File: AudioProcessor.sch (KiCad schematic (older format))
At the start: 17 parts

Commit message: 3v3 über LDO von BMS enablen. Bluetooth hinzugefügt
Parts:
- added J601: AudioJack3_Ground, symbol Connector:AudioJack3_Ground
- added R604, R605, R606, R607: 100R, symbol Device:R_Small
- added R608, R609: 47R, symbol Device:R_Small
- C607, C608, C609, C610: renamed from C?; value 1nF -> 100nF
- gave numbers to parts that had none: 13
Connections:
- net labels added: AUX_DETECT, AUX_GND, BT_GND, BT_LEFT, BT_RIGHT
- net labels removed: BT_L, BT_R
- wire segments 44 -> 63
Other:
- note added: "Folenkondensatoren wegen Akustik"
- note added: "I2C Isolator?"
- note added: "f_cutoff = 1/(100nF*100R) = 15.9kHz"
- moved on the sheet: C603, C604, C605, C606

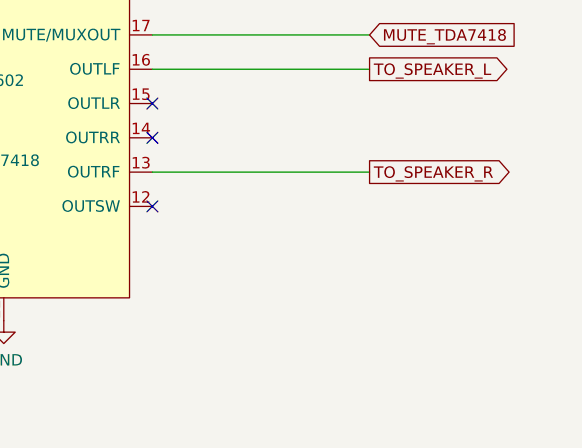
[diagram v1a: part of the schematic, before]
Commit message: power schalter und taser hinzugefügt. Selbsthaltung LDO hinzugefügt. Gain Potis hinzugefügt, Separater Ground für Audio Lines
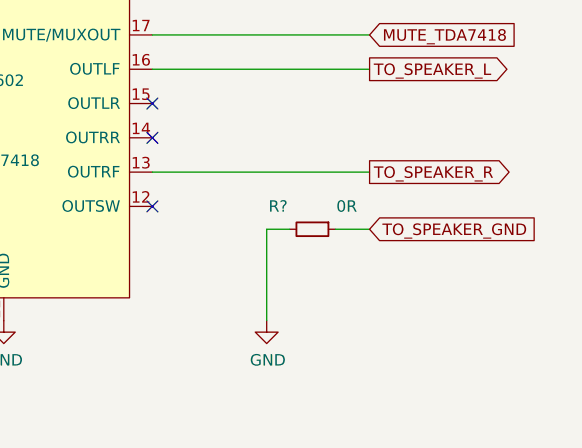
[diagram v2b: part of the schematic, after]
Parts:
- added R?: 0R, symbol Device:R_Small
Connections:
- net labels added: TO_SPEAKER_GND
- wire segments 63 -> 66
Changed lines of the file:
@@
 Wire Wire Line
 	2100 4750 1600 4750
+Text GLabel 9050 5100 2    50   Input ~ 0
+TO_SPEAKER_GND
+$Comp
+L Device:R_Small R?
+U 1 1 5E923218
+P 8800 5100
+F 0 "R?" V 8700 4950 50  0000 C CNN
+F 1 "0R" V 8700 5250 50  0000 C CNN
+F 2 "" H 8800 5100 50  0001 C CNN
+F 3 "~" H 8800 5100 50  0001 C CNN
+	1    8800 5100
+	0    1    1    0
+$EndComp
+Wire Wire Line
+	9050 5100 8900 5100
+$Comp
+L power:GND #PWR?
+U 1 1 5E924643
+P 8600 5500
+F 0 "#PWR?" H 8600 5250 50  0001 C CNN
+F 1 "GND" H 8605 5327 50  0000 C CNN
+F 2 "" H 8600 5500 50  0001 C CNN
+F 3 "" H 8600 5500 50  0001 C CNN
+	1    8600 5500
+	1    0    0    -1
+$EndComp
+Wire Wire Line
+	8700 5100 8600 5100
+Wire Wire Line
+	8600 5100 8600 5500
 $EndSCHEMATC

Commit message: Schaltplan fertig. Fertig für review
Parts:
- removed R?: 0R, symbol Device:R_Small
- added R? (x2): 47K, symbol Device:R_Small
- added R?: DNP, symbol Device:R_Small
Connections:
- net labels added: +3V3, GNDA
- net labels removed: AUX_GND, BT_GND, TO_SPEAKER_GND
- wire segments 66 -> 67
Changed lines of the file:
@@
 Wire Wire Line
 	5900 4050 6350 4050
-$Comp
-L power:GND #PWR0159
-U 1 1 5EA68AB5
-P 7450 5500
-F 0 "#PWR0159" H 7450 5250 50  0001 C CNN
-F 1 "GND" H 7455 5327 50  0000 C CNN
-F 2 "" H 7450 5500 50  0001 C CNN
-F 3 "" H 7450 5500 50  0001 C CNN
-	1    7450 5500
-	1    0    0    -1
-$EndComp
 Wire Wire Line
 	7450 3700 7450 3450
@@
 Text GLabel 9050 4250 2    50   Input ~ 0
 MUTE_TDA7418
-Wire Wire Line
-	9050 4250 8100 4250
 NoConn ~ 8100 4550
 NoConn ~ 8100 4700
@@
 	6650 5350 6650 5550
 $Comp
-L power:GND #PWR0165
-U 1 1 5EACAB6F
-P 6650 5750
-F 0 "#PWR0165" H 6650 5500 50  0001 C CNN
-F 1 "GND" H 6655 5577 50  0000 C CNN
-F 2 "" H 6650 5750 50  0001 C CNN
-F 3 "" H 6650 5750 50  0001 C CNN
-	1    6650 5750
-	1    0    0    -1
-$EndComp
-$Comp
 L power:+9V #PWR0166
 U 1 1 5EACB6B4
@@
 Text Notes 3450 3950 0    89   ~ 0
 I2C Isolator?
-Text GLabel 6250 5750 0    50   Input ~ 0
-BT_GND
 Wire Wire Line
 	6450 5250 6450 5300
@@
 Wire Wire Line
 	6250 5300 6250 5750
-Text GLabel 5850 5650 0    50   Input ~ 0
-AUX_GND
 Wire Wire Line
 	6050 5250 6050 5300
@@
 Wire Wire Line
 	5850 5300 5850 5250
-Wire Wire Line
-	5850 5300 5850 5650
 Connection ~ 5850 5300
 $Comp
@@
 	1    0    0    -1
 $EndComp
-Text GLabel 2100 4850 2    50   Output ~ 0
+Text GLabel 2950 4850 2    50   Output ~ 0
 AUX_DETECT
-Wire Wire Line
-	2100 4850 1600 4850
-Text GLabel 1850 5200 2    50   Output ~ 0
-AUX_GND
-Wire Wire Line
-	1850 5200 1400 5200
 Wire Wire Line
 	1400 5200 1400 5050
@@
 Wire Wire Line
 	2100 4750 1600 4750
-Text GLabel 9050 5100 2    50   Input ~ 0
-TO_SPEAKER_GND
+$Comp
+L power:GNDA #PWR?
+U 1 1 5E90960C
+P 6250 5750
+F 0 "#PWR?" H 6250 5500 50  0001 C CNN
+F 1 "GNDA" H 6255 5577 50  0000 C CNN
+F 2 "" H 6250 5750 50  0001 C CNN
+F 3 "" H 6250 5750 50  0001 C CNN
+	1    6250 5750
+	1    0    0    -1
+$EndComp
+$Comp
+L power:GNDA #PWR?
+U 1 1 5E909649
+P 5850 5750
+F 0 "#PWR?" H 5850 5500 50  0001 C CNN
+F 1 "GNDA" H 5855 5577 50  0000 C CNN
+F 2 "" H 5850 5750 50  0001 C CNN
+F 3 "" H 5850 5750 50  0001 C CNN
+	1    5850 5750
+	1    0    0    -1
+$EndComp
+Wire Wire Line
+	5850 5300 5850 5750
+$Comp
+L power:GND #PWR?
+U 1 1 5E90AB64
+P 6650 5750
+F 0 "#PWR?" H 6650 5500 50  0001 C CNN
+F 1 "GND" H 6655 5577 50  0000 C CNN
+F 2 "" H 6650 5750 50  0001 C CNN
+F 3 "" H 6650 5750 50  0001 C CNN
+	1    6650 5750
+	1    0    0    -1
+$EndComp
+$Comp
+L power:GND #PWR?
+U 1 1 5E90D4CD
+P 7450 5750
+F 0 "#PWR?" H 7450 5500 50  0001 C CNN
+F 1 "GND" H 7455 5577 50  0000 C CNN
+F 2 "" H 7450 5750 50  0001 C CNN
+F 3 "" H 7450 5750 50  0001 C CNN
+	1    7450 5750
+	1    0    0    -1
+$EndComp
+Wire Wire Line
+	7450 5750 7450 5500
 $Comp
 L Device:R_Small R?
-U 1 1 5E923218
-P 8800 5100
-F 0 "R?" V 8700 4950 50  0000 C CNN
-F 1 "0R" V 8700 5250 50  0000 C CNN
-F 2 "" H 8800 5100 50  0001 C CNN
-F 3 "~" H 8800 5100 50  0001 C CNN
-	1    8800 5100
-	0    1    1    0
-$EndComp
-Wire Wire Line
-	9050 5100 8900 5100
+U 1 1 5EB72225
+P 2400 5100
+F 0 "R?" H 2459 5146 50  0000 L CNN
+F 1 "47K" H 2459 5055 50  0000 L CNN
+F 2 "" H 2400 5100 50  0001 C CNN
+F 3 "~" H 2400 5100 50  0001 C CNN
+	1    2400 5100
+	1    0    0    -1
+$EndComp
+Wire Wire Line
+	2400 5000 2400 4850
+Wire Wire Line
+	1600 4850 2400 4850
+Wire Wire Line
+	2950 4850 2400 4850
+Connection ~ 2400 4850
+$Comp
+L power:+3V3 #PWR?
+U 1 1 5EB74D00
+P 2400 5200
+F 0 "#PWR?" H 2400 5050 50  0001 C CNN
+F 1 "+3V3" H 2415 5373 50  0000 C CNN
+F 2 "" H 2400 5200 50  0001 C CNN
+F 3 "" H 2400 5200 50  0001 C CNN
+	1    2400 5200
+	-1   0    0    1
+$EndComp
+$Comp
+L Device:R_Small R?
+U 1 1 5EB80BE5
+P 8450 4150
+F 0 "R?" H 8509 4196 50  0000 L CNN
+F 1 "47K" H 8509 4105 50  0000 L CNN
+F 2 "" H 8450 4150 50  0001 C CNN
+F 3 "~" H 8450 4150 50  0001 C CNN
+	1    8450 4150
+	1    0    0    -1
+$EndComp
+Wire Wire Line
+	8450 4250 8100 4250
+$Comp
+L power:+3V3 #PWR?
+U 1 1 5EB80D40
+P 8450 4050
+F 0 "#PWR?" H 8450 3900 50  0001 C CNN
+F 1 "+3V3" H 8465 4223 50  0000 C CNN
+F 2 "" H 8450 4050 50  0001 C CNN
+F 3 "" H 8450 4050 50  0001 C CNN
+	1    8450 4050
+	1    0    0    -1
+$EndComp
+$Comp
+L Device:R_Small R?
+U 1 1 5EB80DBA
+P 8800 4150
+F 0 "R?" H 8859 4196 50  0000 L CNN
+F 1 "DNP" H 8859 4105 50  0000 L CNN
+F 2 "" H 8800 4150 50  0001 C CNN
+F 3 "~" H 8800 4150 50  0001 C CNN
+	1    8800 4150
+	1    0    0    -1
+$EndComp
 $Comp
 L power:GND #PWR?
-U 1 1 5E924643
-P 8600 5500
-F 0 "#PWR?" H 8600 5250 50  0001 C CNN
-F 1 "GND" H 8605 5327 50  0000 C CNN
-F 2 "" H 8600 5500 50  0001 C CNN
-F 3 "" H 8600 5500 50  0001 C CNN
-	1    8600 5500
-	1    0    0    -1
-$EndComp
-Wire Wire Line
-	8700 5100 8600 5100
-Wire Wire Line
-	8600 5100 8600 5500
+U 1 1 5EB80ED7
+P 8800 4050
+F 0 "#PWR?" H 8800 3800 50  0001 C CNN
+F 1 "GND" H 8805 3877 50  0000 C CNN
+F 2 "" H 8800 4050 50  0001 C CNN
+F 3 "" H 8800 4050 50  0001 C CNN
+	1    8800 4050
+	-1   0    0    1
+$EndComp
+Connection ~ 8450 4250
+Wire Wire Line
+	8450 4250 8800 4250
+Connection ~ 8800 4250
+Wire Wire Line
+	8800 4250 9050 4250
+$Comp
+L power:GNDA #PWR?
+U 1 1 5ECAADBB
+P 1400 5200
+F 0 "#PWR?" H 1400 4950 50  0001 C CNN
+F 1 "GNDA" H 1405 5027 50  0000 C CNN
+F 2 "" H 1400 5200 50  0001 C CNN
+F 3 "" H 1400 5200 50  0001 C CNN
+	1    1400 5200
+	1    0    0    -1
+$EndComp
 $EndSCHEMATC

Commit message: Footprintzuordnung angefangen
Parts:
- added J602: Conn_02x01, symbol Connector_Generic:Conn_02x01
- R602: value 35K? -> 32K5
- gave numbers to parts that had none: 3
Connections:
- wire segments 67 -> 69
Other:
- moved on the sheet: R610
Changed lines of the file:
@@
 Text GLabel 4750 4450 0    50   Input ~ 0
 BT_RIGHT
-Text GLabel 4750 4600 0    50   Input ~ 0
-AUX_L
-Text GLabel 4750 4750 0    50   Input ~ 0
-AUX_R
 Wire Wire Line
 	4850 4300 4750 4300
@@
 Wire Wire Line
 	4750 4600 4850 4600
-Wire Wire Line
-	5150 4750 4750 4750
 Text GLabel 9050 4400 2    50   Output ~ 0
 TO_SPEAKER_L
@@
 P 4550 2150
 F 0 "R602" H 4609 2196 50  0000 L CNN
-F 1 "35K?" H 4609 2105 50  0000 L CNN
+F 1 "32K5" H 4609 2105 50  0000 L CNN
 F 2 "" H 4550 2150 50  0001 C CNN
 F 3 "~" H 4550 2150 50  0001 C CNN
@@
 L power:+9V #PWR0169
 U 1 1 5EAD4B38
-P 5300 2000
-F 0 "#PWR0169" H 5300 1850 50  0001 C CNN
-F 1 "+9V" H 5315 2173 50  0000 C CNN
-F 2 "" H 5300 2000 50  0001 C CNN
-F 3 "" H 5300 2000 50  0001 C CNN
-	1    5300 2000
+P 6050 2000
+F 0 "#PWR0169" H 6050 1850 50  0001 C CNN
+F 1 "+9V" H 6065 2173 50  0000 C CNN
+F 2 "" H 6050 2000 50  0001 C CNN
+F 3 "" H 6050 2000 50  0001 C CNN
+	1    6050 2000
 	1    0    0    -1
 $EndComp
@@
 L Connector:AudioJack3_Ground J601
 U 1 1 5E85FCC9
-P 1400 4750
-F 0 "J601" H 1380 5075 50  0000 C CNN
-F 1 "AudioJack3_Ground" H 1380 4984 50  0000 C CNN
-F 2 "" H 1400 4750 50  0001 C CNN
-F 3 "~" H 1400 4750 50  0001 C CNN
-	1    1400 4750
-	1    0    0    -1
-$EndComp
-Text GLabel 2950 4850 2    50   Output ~ 0
+P 3050 4750
+F 0 "J601" H 3030 5075 50  0000 C CNN
+F 1 "AudioJack3_Ground" H 3030 4984 50  0000 C CNN
+F 2 "" H 3050 4750 50  0001 C CNN
+F 3 "~" H 3050 4750 50  0001 C CNN
+	1    3050 4750
+	1    0    0    -1
+$EndComp
+Text GLabel 3500 4850 2    50   Output ~ 0
 AUX_DETECT
 Wire Wire Line
-	1400 5200 1400 5050
-Text GLabel 2100 4650 2    50   Output ~ 0
-AUX_L
-Wire Wire Line
-	2100 4650 1600 4650
-Text GLabel 2100 4750 2    50   Output ~ 0
-AUX_R
-Wire Wire Line
-	2100 4750 1600 4750
-$Comp
-L power:GNDA #PWR?
+	3050 5200 3050 5050
+$Comp
+L power:GNDA #PWR0604
 U 1 1 5E90960C
 P 6250 5750
-F 0 "#PWR?" H 6250 5500 50  0001 C CNN
+F 0 "#PWR0604" H 6250 5500 50  0001 C CNN
 F 1 "GNDA" H 6255 5577 50  0000 C CNN
 F 2 "" H 6250 5750 50  0001 C CNN
@@
 $EndComp
 $Comp
-L power:GNDA #PWR?
+L power:GNDA #PWR0603
 U 1 1 5E909649
 P 5850 5750
-F 0 "#PWR?" H 5850 5500 50  0001 C CNN
+F 0 "#PWR0603" H 5850 5500 50  0001 C CNN
 F 1 "GNDA" H 5855 5577 50  0000 C CNN
 F 2 "" H 5850 5750 50  0001 C CNN
@@
 	5850 5300 5850 5750
 $Comp
-L power:GND #PWR?
+L power:GND #PWR0605
 U 1 1 5E90AB64
 P 6650 5750
-F 0 "#PWR?" H 6650 5500 50  0001 C CNN
+F 0 "#PWR0605" H 6650 5500 50  0001 C CNN
 F 1 "GND" H 6655 5577 50  0000 C CNN
 F 2 "" H 6650 5750 50  0001 C CNN
@@
 $EndComp
 $Comp
-L power:GND #PWR?
+L power:GND #PWR0606
 U 1 1 5E90D4CD
 P 7450 5750
-F 0 "#PWR?" H 7450 5500 50  0001 C CNN
+F 0 "#PWR0606" H 7450 5500 50  0001 C CNN
 F 1 "GND" H 7455 5577 50  0000 C CNN
 F 2 "" H 7450 5750 50  0001 C CNN
@@
 	7450 5750 7450 5500
 $Comp
-L Device:R_Small R?
+L Device:R_Small R610
 U 1 1 5EB72225
-P 2400 5100
-F 0 "R?" H 2459 5146 50  0000 L CNN
-F 1 "47K" H 2459 5055 50  0000 L CNN
-F 2 "" H 2400 5100 50  0001 C CNN
-F 3 "~" H 2400 5100 50  0001 C CNN
-	1    2400 5100
-	1    0    0    -1
-$EndComp
-Wire Wire Line
-	2400 5000 2400 4850
-Wire Wire Line
-	1600 4850 2400 4850
-Wire Wire Line
-	2950 4850 2400 4850
-Connection ~ 2400 4850
-$Comp
-L power:+3V3 #PWR?
+P 3400 5100
+F 0 "R610" H 3459 5146 50  0000 L CNN
+F 1 "47K" H 3459 5055 50  0000 L CNN
+F 2 "" H 3400 5100 50  0001 C CNN
+F 3 "~" H 3400 5100 50  0001 C CNN
+	1    3400 5100
+	1    0    0    -1
+$EndComp
+Wire Wire Line
+	3400 5000 3400 4850
+Wire Wire Line
+	3250 4850 3400 4850
+$Comp
+L power:+3V3 #PWR0602
 U 1 1 5EB74D00
-P 2400 5200
-F 0 "#PWR?" H 2400 5050 50  0001 C CNN
-F 1 "+3V3" H 2415 5373 50  0000 C CNN
-F 2 "" H 2400 5200 50  0001 C CNN
-F 3 "" H 2400 5200 50  0001 C CNN
-	1    2400 5200
+P 3400 5200
+F 0 "#PWR0602" H 3400 5050 50  0001 C CNN
+F 1 "+3V3" H 3415 5373 50  0000 C CNN
+F 2 "" H 3400 5200 50  0001 C CNN
+F 3 "" H 3400 5200 50  0001 C CNN
+	1    3400 5200
 	-1   0    0    1
 $EndComp
 $Comp
-L Device:R_Small R?
+L Device:R_Small R611
 U 1 1 5EB80BE5
 P 8450 4150
-F 0 "R?" H 8509 4196 50  0000 L CNN
+F 0 "R611" H 8509 4196 50  0000 L CNN
 F 1 "47K" H 8509 4105 50  0000 L CNN
 F 2 "" H 8450 4150 50  0001 C CNN
@@
 	8450 4250 8100 4250
 $Comp
-L power:+3V3 #PWR?
+L power:+3V3 #PWR0607
 U 1 1 5EB80D40
 P 8450 4050
-F 0 "#PWR?" H 8450 3900 50  0001 C CNN
+F 0 "#PWR0607" H 8450 3900 50  0001 C CNN
 F 1 "+3V3" H 8465 4223 50  0000 C CNN
 F 2 "" H 8450 4050 50  0001 C CNN
@@
 $EndComp
 $Comp
-L Device:R_Small R?
+L Device:R_Small R612
 U 1 1 5EB80DBA
 P 8800 4150
-F 0 "R?" H 8859 4196 50  0000 L CNN
+F 0 "R612" H 8859 4196 50  0000 L CNN
 F 1 "DNP" H 8859 4105 50  0000 L CNN
 F 2 "" H 8800 4150 50  0001 C CNN
@@
 $EndComp
 $Comp
-L power:GND #PWR?
+L power:GND #PWR0608
 U 1 1 5EB80ED7
 P 8800 4050
-F 0 "#PWR?" H 8800 3800 50  0001 C CNN
+F 0 "#PWR0608" H 8800 3800 50  0001 C CNN
 F 1 "GND" H 8805 3877 50  0000 C CNN
 F 2 "" H 8800 4050 50  0001 C CNN
@@
 	8800 4250 9050 4250
 $Comp
-L power:GNDA #PWR?
+L power:GNDA #PWR0601
 U 1 1 5ECAADBB
-P 1400 5200
-F 0 "#PWR?" H 1400 4950 50  0001 C CNN
-F 1 "GNDA" H 1405 5027 50  0000 C CNN
-F 2 "" H 1400 5200 50  0001 C CNN
-F 3 "" H 1400 5200 50  0001 C CNN
-	1    1400 5200
-	1    0    0    -1
-$EndComp
+P 3050 5200
+F 0 "#PWR0601" H 3050 4950 50  0001 C CNN
+F 1 "GNDA" H 3055 5027 50  0000 C CNN
+F 2 "" H 3050 5200 50  0001 C CNN
+F 3 "" H 3050 5200 50  0001 C CNN
+	1    3050 5200
+	1    0    0    -1
+$EndComp
+Wire Wire Line
+	3500 4850 3400 4850
+Connection ~ 3400 4850
+Wire Wire Line
+	4750 4600 4750 4650
+Wire Wire Line
+	3250 4650 4750 4650
+Wire Wire Line
+	3250 4750 5150 4750
+Text Label 3750 4650 0    50   ~ 0
+AUX_L
+Text Label 3750 4750 0    50   ~ 0
+AUX_R
+$Comp
+L Connector_Generic:Conn_02x01 J602
+U 1 1 5EC2DF69
+P 5500 2000
+F 0 "J602" H 5550 2217 50  0000 C CNN
+F 1 "Conn_02x01" H 5550 2126 50  0000 C CNN
+F 2 "" H 5500 2000 50  0001 C CNN
+F 3 "~" H 5500 2000 50  0001 C CNN
+	1    5500 2000
+	1    0    0    -1
+$EndComp
+Wire Wire Line
+	6050 2000 5800 2000
+$Comp
+L power:PWR_FLAG #FLG0112
+U 1 1 5EC34444
+P 6400 2000
+F 0 "#FLG0112" H 6400 2075 50  0001 C CNN
+F 1 "PWR_FLAG" H 6400 2174 50  0000 C CNN
+F 2 "" H 6400 2000 50  0001 C CNN
+F 3 "~" H 6400 2000 50  0001 C CNN
+	1    6400 2000
+	1    0    0    -1
+$EndComp
+Wire Wire Line
+	6400 2000 6050 2000
+Connection ~ 6050 2000
 $EndSCHEMATC
